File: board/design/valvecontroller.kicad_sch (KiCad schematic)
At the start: 11 parts, among them J1 Jack-DC, J2 Jack-DC, K1 G5V-1, Q1 BT169G, SW1 SW_DIP_x01, U1 ${SIM.PARAMS}

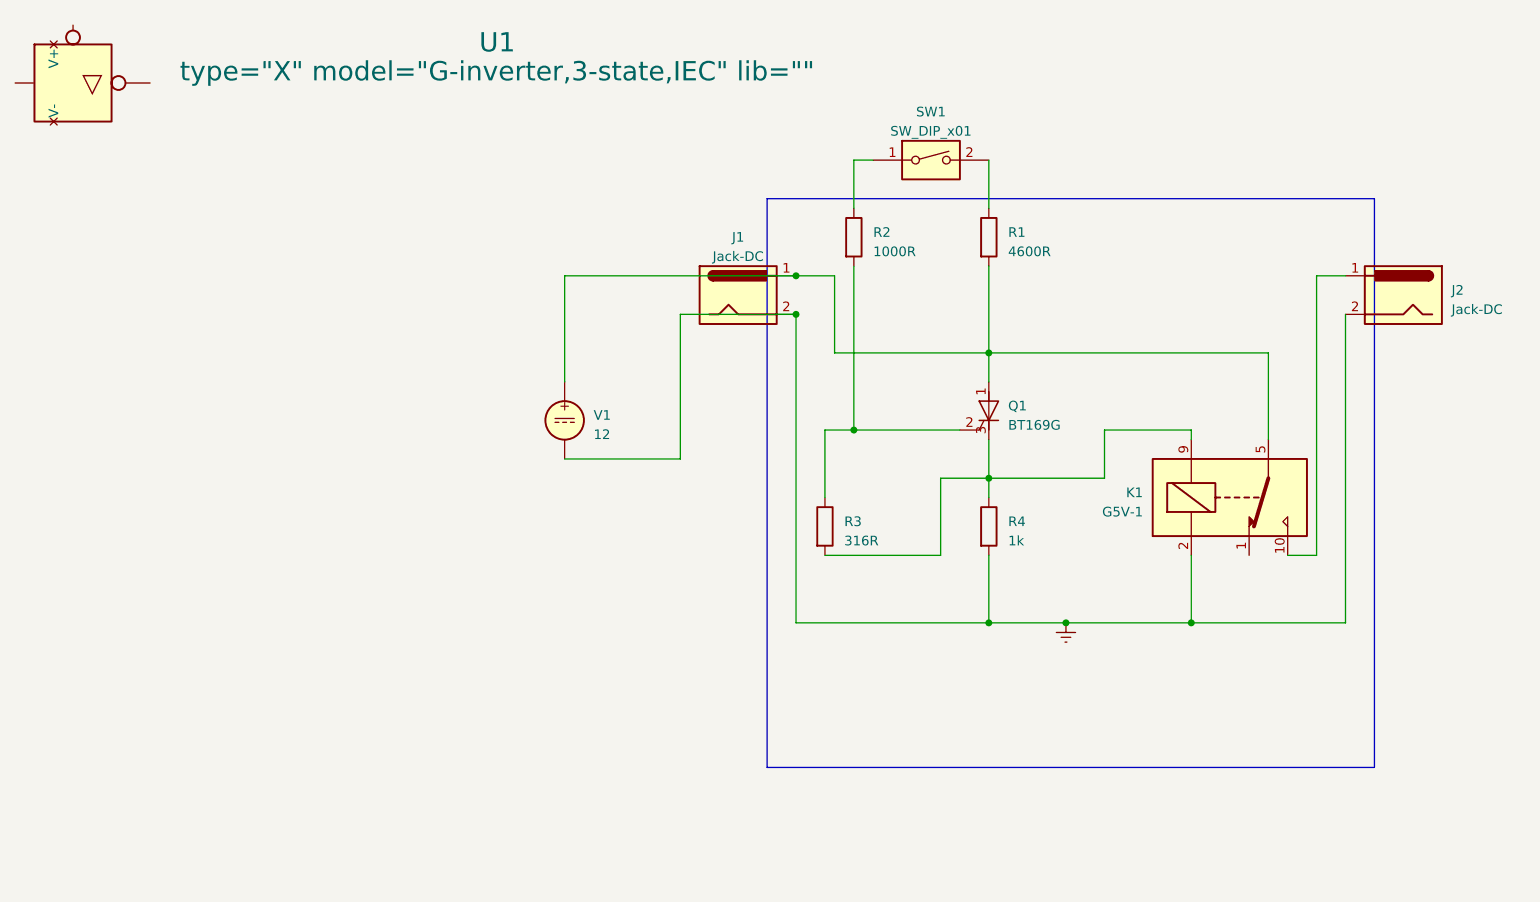
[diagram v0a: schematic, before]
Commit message: change to schmitt trigger
this is (by mistake) for a closing fluid level switch
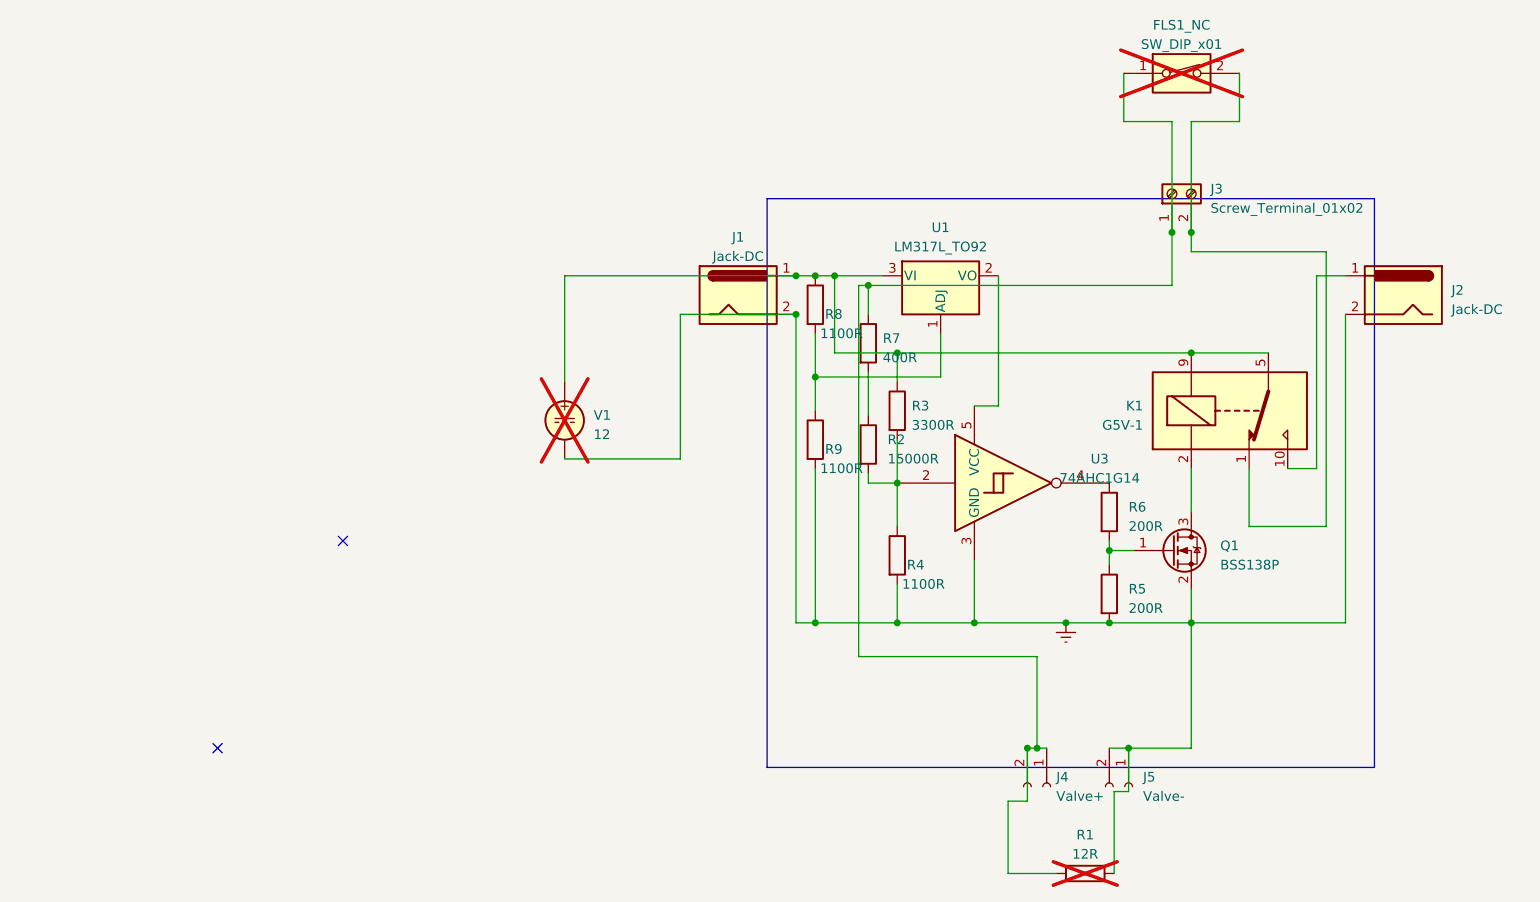
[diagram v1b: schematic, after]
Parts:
- removed Q1: BT169G, Package_TO_SOT_THT:TO-92_Inline, symbol Triac_Thyristor:BT169G
- removed U1: ${SIM.PARAMS}, symbol PCM_Generic:G-inverter,3-state,IEC
- added J3: Screw_Terminal_01x02, symbol Connector:Screw_Terminal_01x02
- added J4: Valve+, symbol Connector:Conn_01x02_Socket
- added J5: Valve-, symbol Connector:Conn_01x02_Socket
- added Q1: BSS138P, Package_TO_SOT_SMD:SOT-23, symbol Transistor_FET:BSS138
- added R5, R6: 200R, symbol Device:R
- added R7: 400R, symbol Device:R
- added R8, R9: 1100R, symbol Device:R
- added U1: LM317L_TO92, Package_TO_SOT_THT:TO-92_Inline, symbol Regulator_Linear:LM317L_TO92
- added U3: 74AHC1G14, symbol 74xGxx:74AHC1G14
- FLS1_NC: renamed from SW1; now not fitted; now left out of the parts list
- R1: value 4600R -> 12R; now not fitted; now left out of the parts list
- R2: value 1000R -> 15000R
- R3: value 316R -> 3300R
- R4: value 1k -> 1100R
- V1: now not fitted; now left out of the parts list
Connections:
- net Earth: now also R1.2, J5.1 (Pin_1), J5.2 (Pin_2), Q1.2 (S), R5.2, R9.2, U3.3 (GND); no longer K1.2
- net at R1.1: now also FLS1_NC.1, J3.1 (Pin_1), J4.1 (Pin_1), J4.2 (Pin_2), R7.1; no longer FLS1_NC.2
- net at J1.1, K1.5, K1.6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: now also K1.9, R3.1, R8.1, U1.3 (VI); no longer R1.2
- net at K1.1: now also FLS1_NC.2, J3.2 (Pin_2)
- net at R3.2, R4.1: now also R2.2, U3.2; no longer K1.9
- net at R2.1: now also R7.2; no longer FLS1_NC.1
- new net: K1.2, Q1.3 (D)
- new net: R8.2, R9.1, U1.1 (ADJ)
- new net: Q1.1 (G), R5.1, R6.2
- new net: R6.1, U3.4
- new net: U1.2 (VO), U3.5 (VCC)
- no-connect marks 0 -> 2
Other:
- moved on the sheet: K1

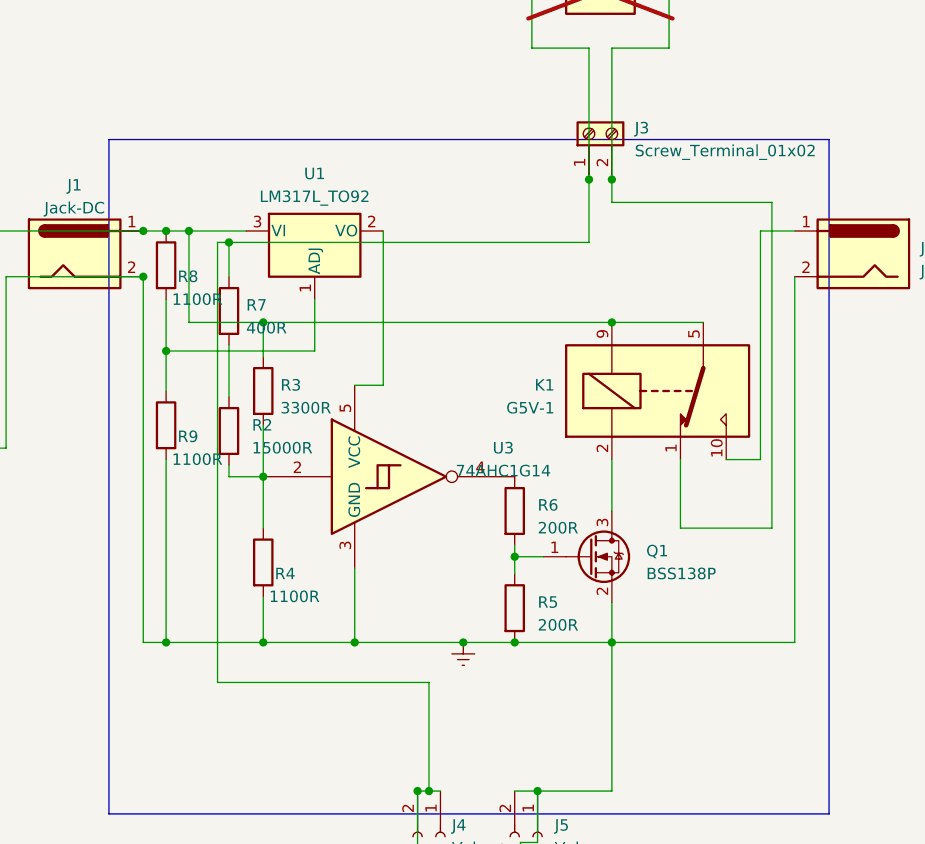
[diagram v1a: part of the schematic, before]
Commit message: fix relay model
can now simulate a relay
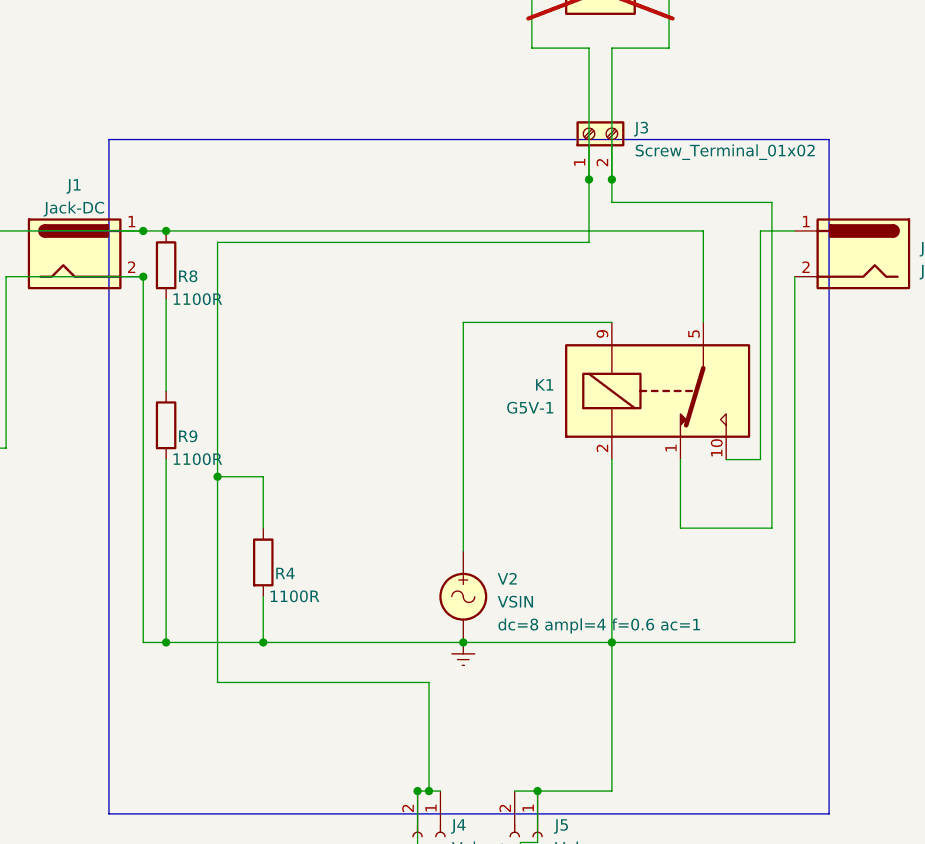
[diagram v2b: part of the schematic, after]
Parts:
- removed Q1: BSS138P, Package_TO_SOT_SMD:SOT-23, symbol Transistor_FET:BSS138
- removed R2: 15000R, symbol Device:R
- removed R3: 3300R, symbol Device:R
- removed R5, R6: 200R, symbol Device:R
- removed R7: 400R, symbol Device:R
- removed U1: LM317L_TO92, Package_TO_SOT_THT:TO-92_Inline, symbol Regulator_Linear:LM317L_TO92
- removed U3: 74AHC1G14, symbol 74xGxx:74AHC1G14
- added V2: VSIN, symbol Simulation_SPICE:VSIN
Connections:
- net Earth: now also K1.2, V2.2
- net at R4.1: now also FLS1_NC.1, J3.1 (Pin_1), J4.1 (Pin_1), J4.2 (Pin_2), R1.1
- net at J1.1, K1.5, K1.6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: no longer K1.9
- new net: K1.9, V2.1
